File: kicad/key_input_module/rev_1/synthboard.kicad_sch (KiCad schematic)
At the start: 51 parts, among them J1 Connect to Upper Module/Mothe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, J2 Connect to Lower Module, J3 Modular Inputs, SW1 SW_Push, SW10 SW_Push, SW11 SW_Push, SW12 SW_Push, SW2 SW_Push, SW3 SW_Push, SW4 SW_Push, SW5 SW_Push, SW6 SW_Push, SW7 SW_Push, SW8 SW_Push, SW9 SW_Push, U1 74HC165, U2 74HC165

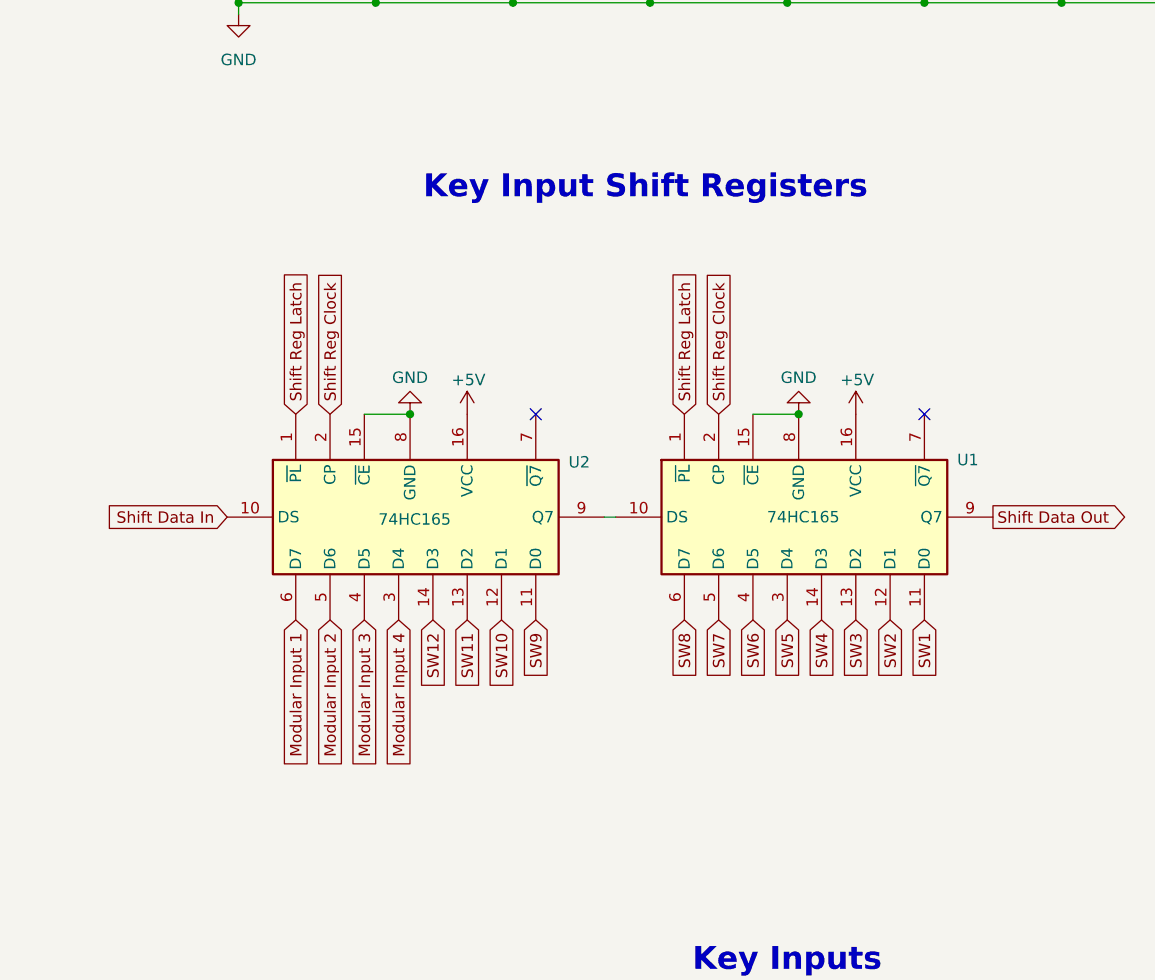
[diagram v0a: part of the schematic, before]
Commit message: Updated README and file structure
Added recent news about PCBs to the README, cleaned up how the local project library is handled in KiCad, and changed sub-folder structure for the KiCad folder.
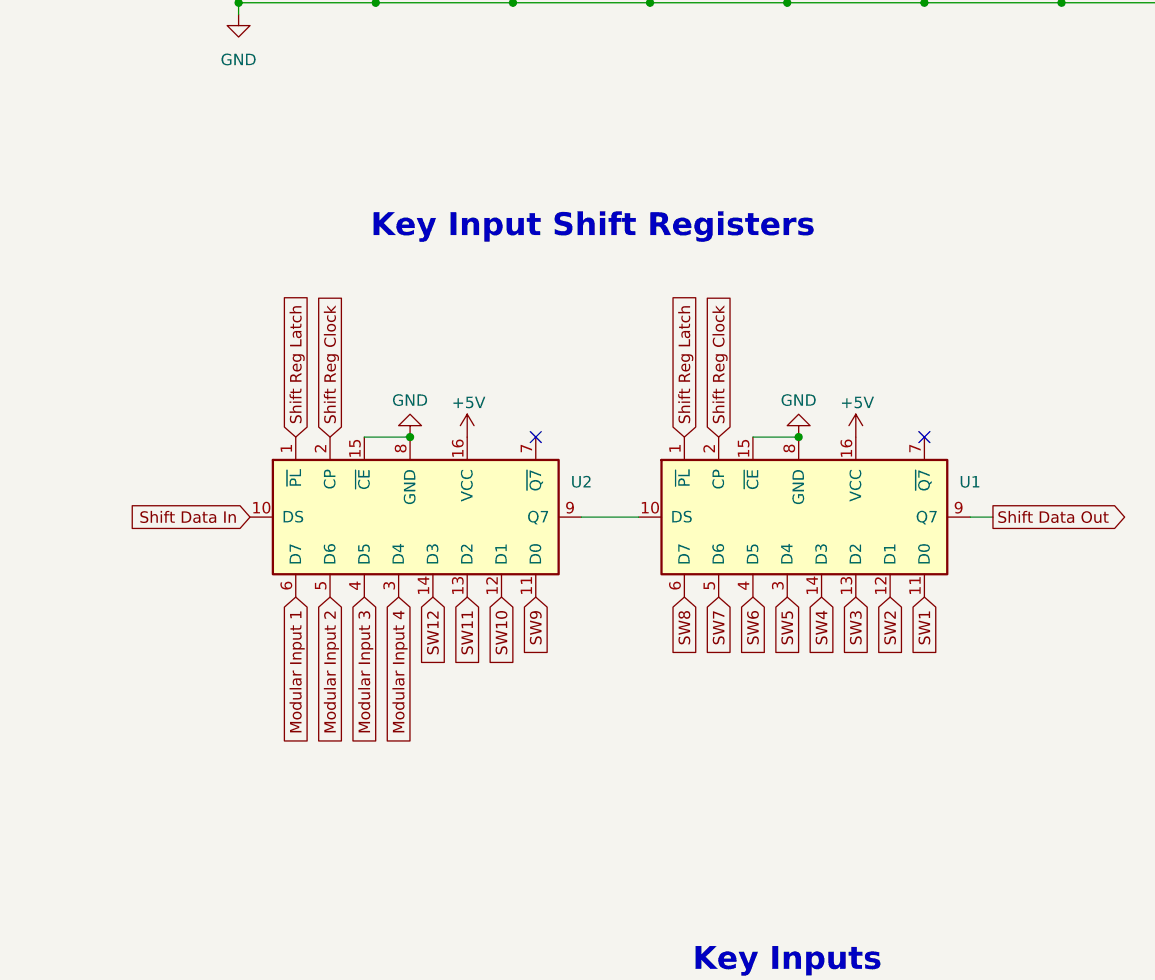
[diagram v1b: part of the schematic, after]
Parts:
- removed U1, U2: 74HC165, 74HC165D_653:SOIC127P600X175-16N, symbol 74xx:74HC165
- added U1, U2: 74HC165D_653, synthboard:SOIC127P600X175-16N, symbol synthboard:74HC165D_653
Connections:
- net +5V: now also U1.16 (VCC), U2.16 (VCC)
- net GND: now also U1.15 (~{CE}), U1.8 (GND), U2.15 (~{CE}), U2.8 (GND)
- net Modular Input 1: now also U2.6 (D7)
- net Modular Input 2: now also U2.5 (D6)
- net Modular Input 3: now also U2.4 (D5)
- net Modular Input 4: now also U2.3 (D4)
- net SW1: now also U1.11 (D0)
- net SW10: now also U2.12 (D1)
- net SW11: now also U2.13 (D2)
- net SW12: now also U2.14 (D3)
- net SW2: now also U1.12 (D1)
- net SW3: now also U1.13 (D2)
- net SW4: now also U1.14 (D3)
- net SW5: now also U1.3 (D4)
- net SW6: now also U1.4 (D5)
- net SW7: now also U1.5 (D6)
- net SW8: now also U1.6 (D7)
- net SW9: now also U2.11 (D0)
- net Shift Data In: now also U2.10 (DS)
- net Shift Data Out: now also U1.9 (Q7)
- net Shift Reg Clock: now also U1.2 (CP), U2.2 (CP)
- net Shift Reg Latch: now also U1.1 (~{PL}), U2.1 (~{PL})
- new net: U1.10 (DS), U2.9 (Q7)
